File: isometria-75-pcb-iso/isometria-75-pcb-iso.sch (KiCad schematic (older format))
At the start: 31 parts, among them J101 USB, J102 SPI, Q101 AO3400A, SW101 RST, SW102 BOOT, U101 XC6206P332MR, U102 STM32F072CBTx

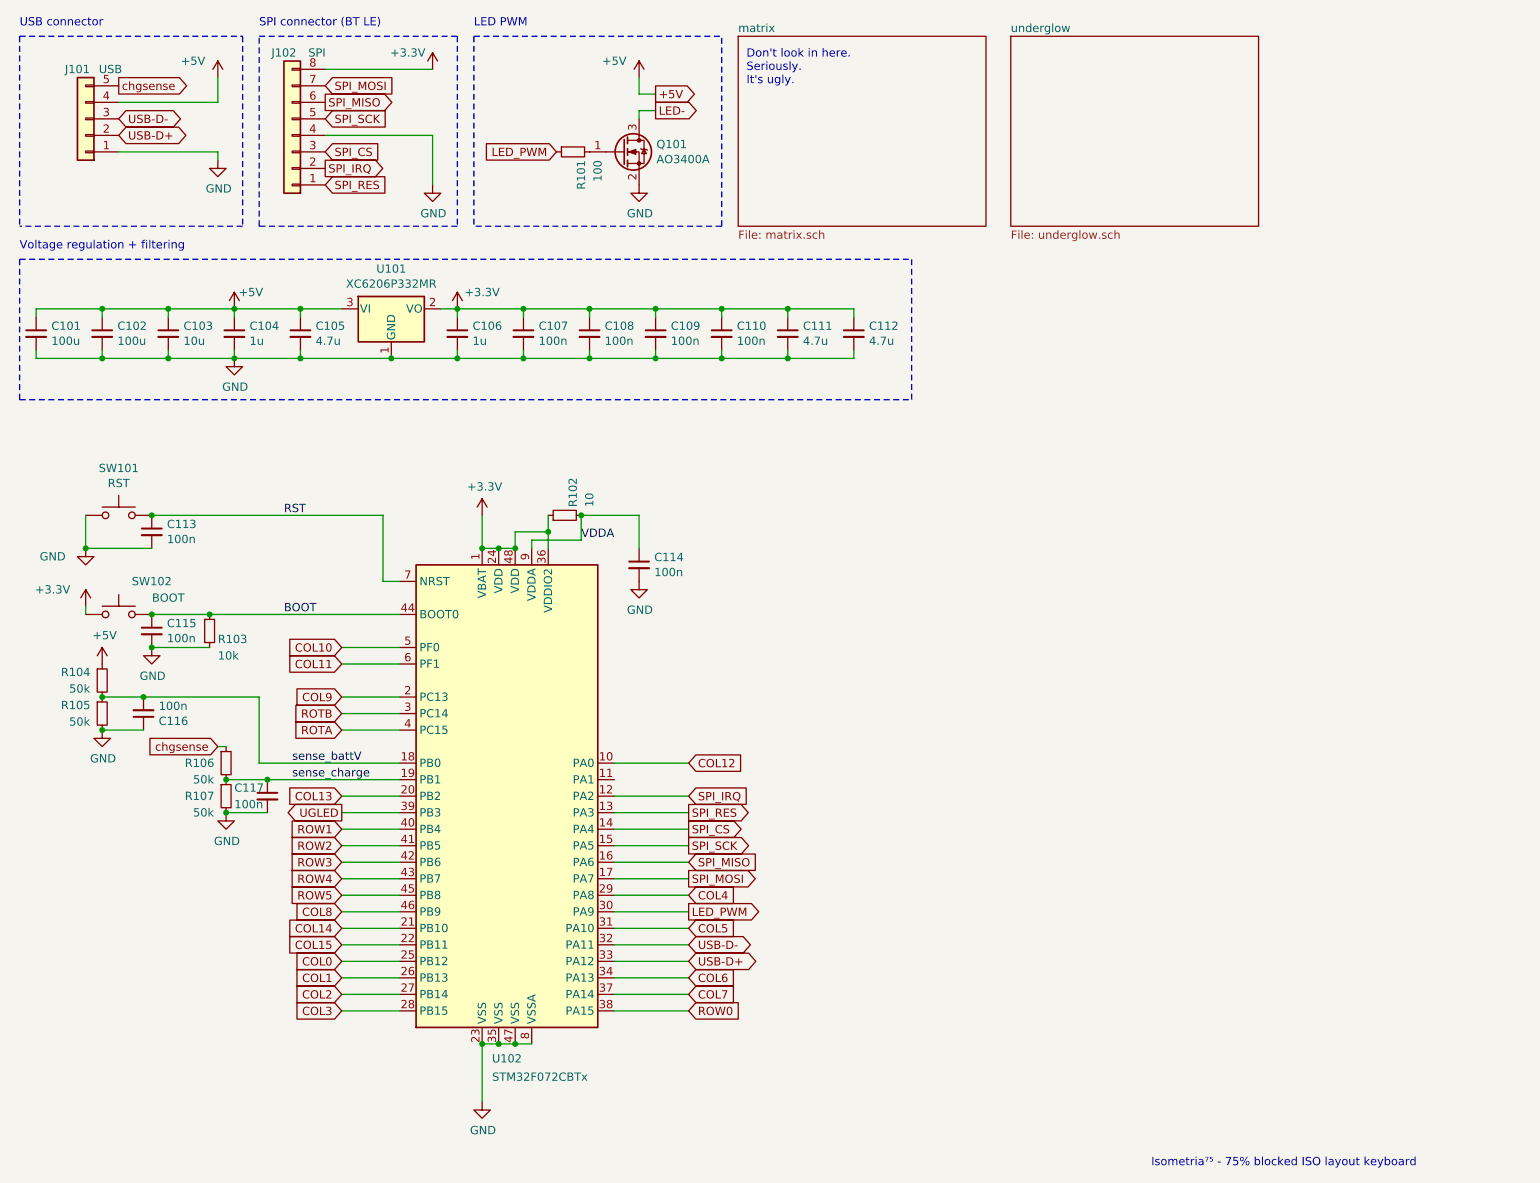
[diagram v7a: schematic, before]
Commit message: routed an unused GPIO to a solder pad
could be used for possible expansion
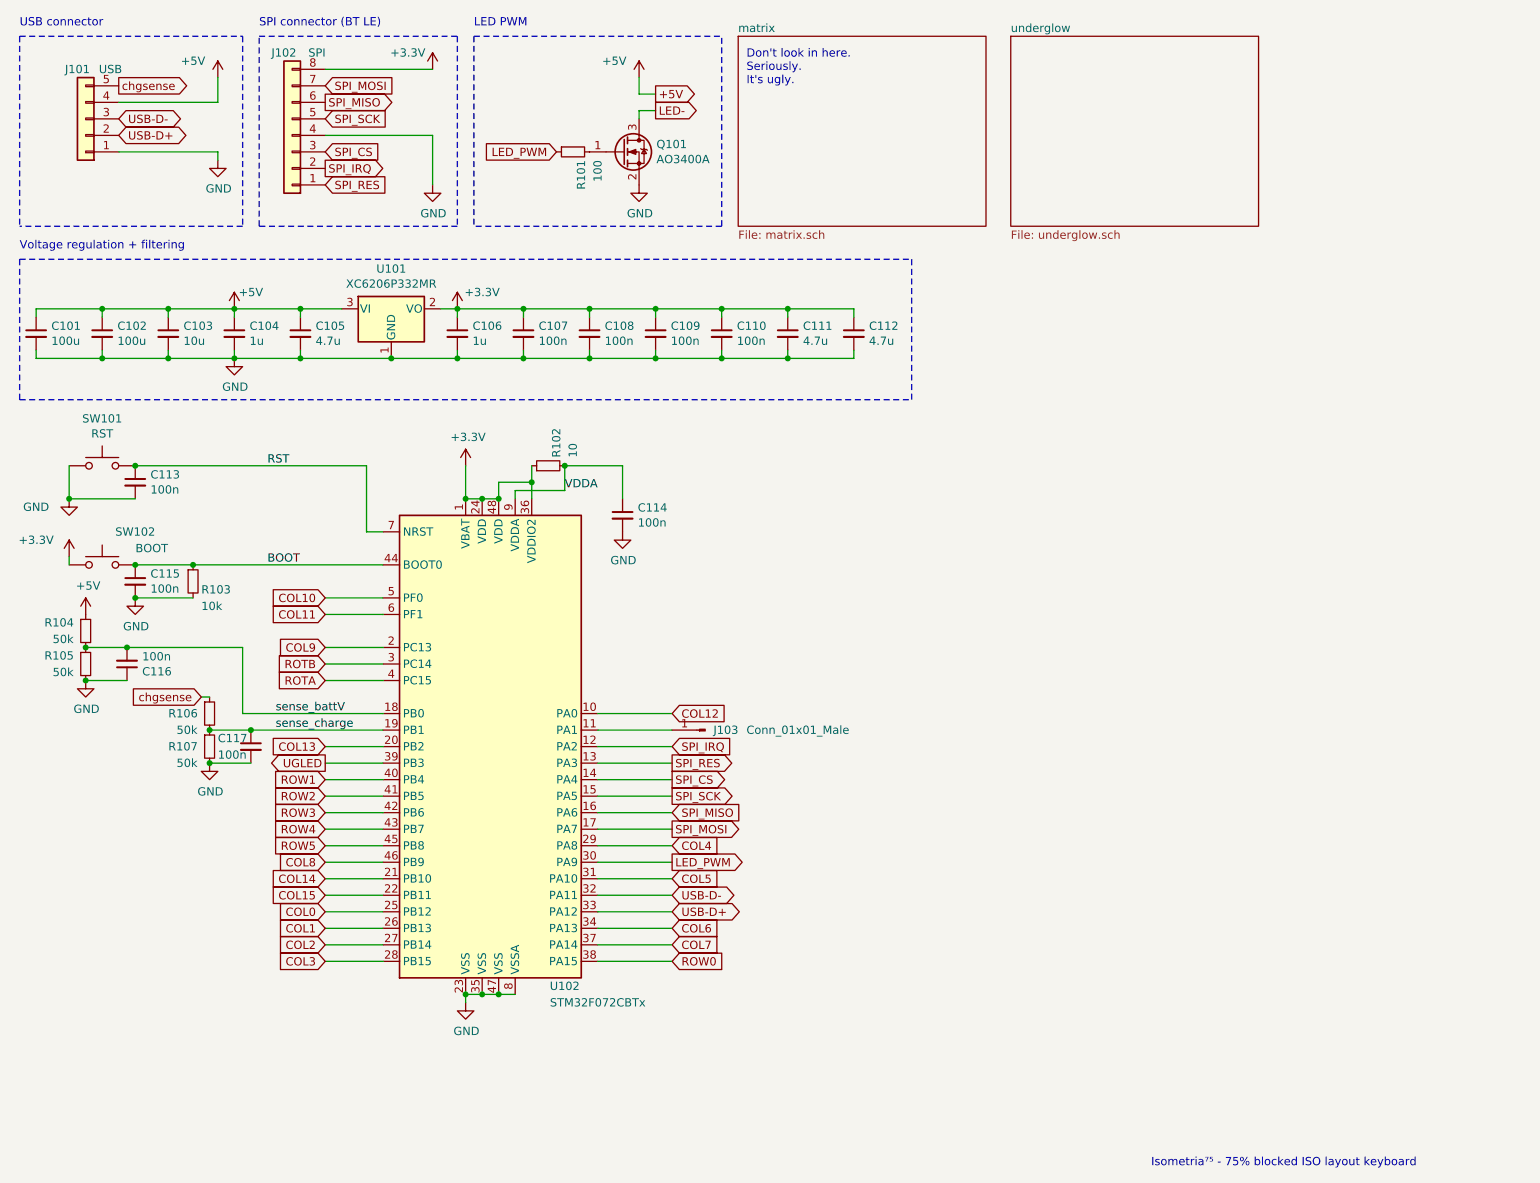
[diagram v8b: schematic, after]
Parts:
- added J103: Conn_01x01_Male, Connector_PinHeader_2.54mm:PinHeader_1x01_P2.54mm_Vertical, symbol Connector:Conn_01x01_Male
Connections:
- net at U102.11 (PA1): now also J103.1 (Pin_1)
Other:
- moved on the sheet: C113, C114, C115, C116, C117, R102, R103, R104, R105, R106, R107, SW101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
